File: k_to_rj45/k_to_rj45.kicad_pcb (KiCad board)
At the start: 2 copper layers, 57.2 x 76.2 mm, 13 parts, among them J1 Conn_01x01_Female, J2 Conn_01x01_Female, J3 Conn_01x01_Female, J4 Conn_01x01_Female, J5 Conn_01x01_Female, J6 RJ45_Shielded, J7 Conn_01x01_Female, J8 Conn_01x01_Female, SW1 SW_SPDT

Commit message: rev3 on contact checker boards
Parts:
- added REF**: KiCad-Logo2_5mm_SilkScreen, Symbol:KiCad-Logo2_5mm_SilkScreen, F.Cu at (114.3, 85.7)
- LOGO1, LOGO2: footprint custom_footprints:logo_small -> custom_footprints:logo
- SW1: value SW_SPDT -> SW_SPDT_MSM
- moved LOGO1 13.1 mm to (106.0, 73.0), turned to -90 degrees
- moved LOGO2 13.1 mm to (106.0, 73.0), turned to 90 degrees
- moved REF** 1.27 mm to (114.3, 85.7)
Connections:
- J6 pad 6: GNDPWR -> /GUARD
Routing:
- net /GUARD: track 47.2 -> 70.5 mm
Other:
- board text added: "gXXXXXXX"
- board text removed: "g3d57883"

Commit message: update silk
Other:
- board text added: "gd87d8d8"
- board text removed: "gXXXXXXX"

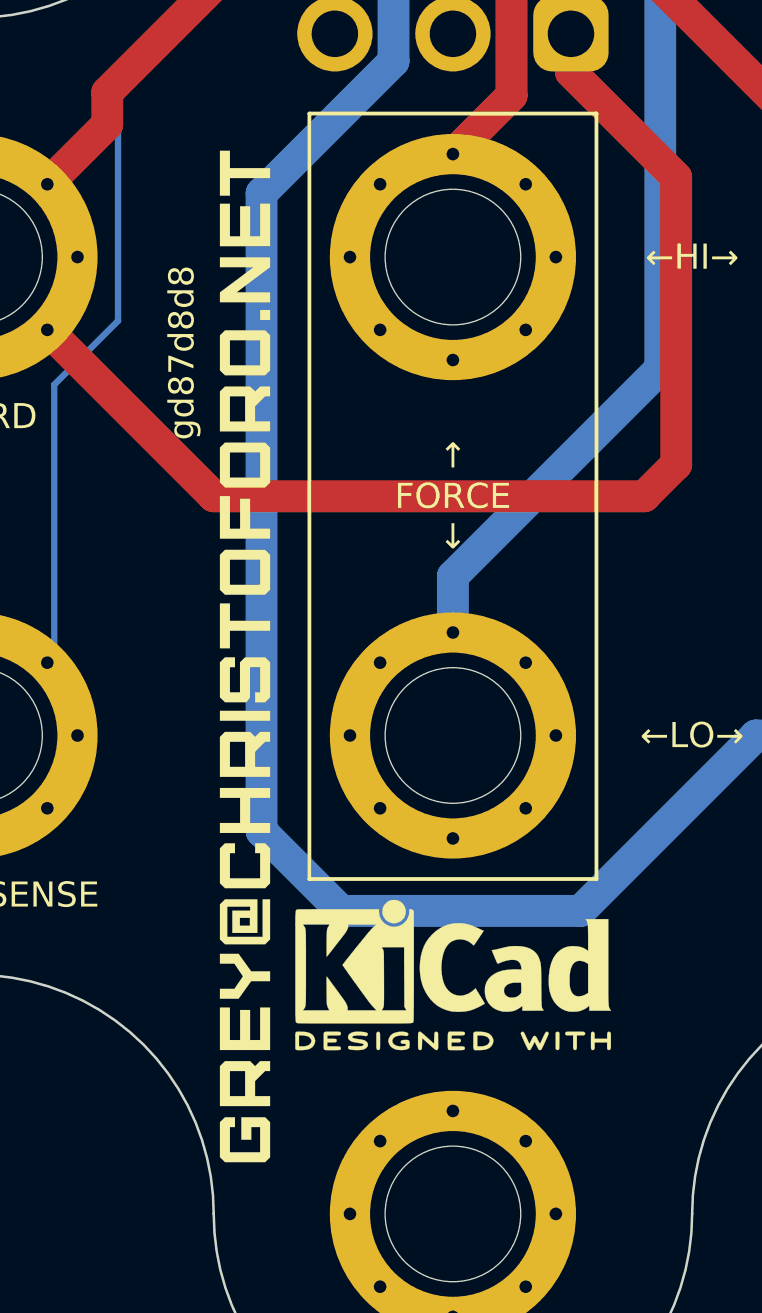
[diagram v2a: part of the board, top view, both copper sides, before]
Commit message: new holder pcbs
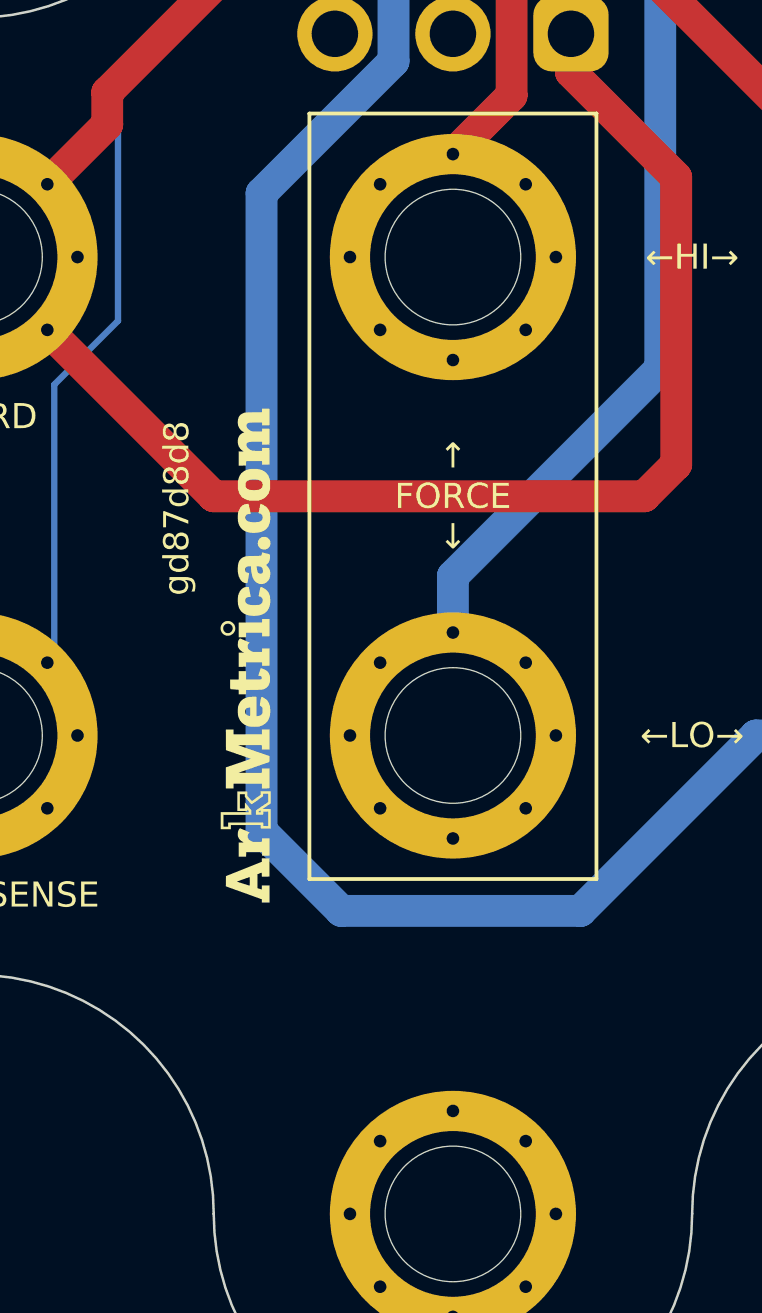
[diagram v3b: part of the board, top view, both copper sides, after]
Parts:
- removed the REF** at (114.3, 85.7) (x2)
- LOGO1, LOGO2: footprint custom_footprints:logo -> custom_footprints:site_small

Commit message: update silk
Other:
- board text added: "b8007ef"
- board text removed: "gd87d8d8"
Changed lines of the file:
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@@
     (effects (font (size 1 1) (thickness 0.15)) (justify mirror))
   )
-  (gr_text "gd87d8d8" (at 103.505 79.15 90) (layer "B.SilkS")
+  (gr_text "b8007ef" (at 103.505 79.15 90) (layer "B.SilkS")
     (effects (font (size 1 1) (thickness 0.15)) (justify mirror))
   )
@@
     (effects (font (size 1 1) (thickness 0.15)))
   )
-  (gr_text "gd87d8d8" (at 103.3 67.15 90) (layer "F.SilkS")
+  (gr_text "b8007ef" (at 103.3 67.15 90) (layer "F.SilkS")
     (effects (font (size 1 1) (thickness 0.15)))
   )

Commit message: fix up rj45 pad numbering
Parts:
- J6: footprint custom_footprints:RJ45_TE_100616-1_vertical_shield -> custom_footprints:RJ45_TE_100616
- LOGO1, LOGO2: footprint custom_footprints:site_small -> custom_footprints:logo
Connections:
- J6 pad 1: /HI_FORCE -> GNDPWR
- J6 pad 2: /HI_SENSE -> GNDPWR
- J6 pad 3: /LO_SENSE -> /GUARD
- J6 pad 4: /LO_FORCE -> /GUARD_SENSE
- J6 pad 5: /GUARD_SENSE -> /LO_FORCE
- J6 pad 6: /GUARD -> /LO_SENSE
- J6 pad 7: GNDPWR -> /HI_SENSE
- J6 pad 8: GNDPWR -> /HI_FORCE

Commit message: shrink steps, add double rj45 to cc
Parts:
- removed REF**: Symbol_Attention_CopperTop_Small, Symbol:Symbol_Attention_CopperTop_Small
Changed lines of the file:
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@@
   (net 7 "/GUARD")
   (net 8 "/SHIELD")
-  (footprint "Symbol:Symbol_Attention_CopperTop_Small" (layer "F.Cu")
-    (at 114.3 34.925)
-    (descr "Symbol, Attention, Copper Top, Small,")
-    (tags "Symbol, Attention, Copper Top, Small,")
-    (attr exclude_from_pos_files exclude_from_bom)
-    (fp_text reference "REF**" (at -0.127 -5.715) (layer "F.SilkS") hide
-        (effects (font (size 1 1) (thickness 0.15)))
-    )
-    (fp_text value "Symbol_Attention_CopperTop_Small" (at -0.381 4.572) (layer "F.Fab")
-        (effects (font (size 1 1) (thickness 0.15)))
-    )
-    (fp_line (start -4.699 2.794) (end 0 -4.191)
-      (stroke (width 0.381) (type solid)) (layer "F.SilkS"))
-    (fp_line (start -0.508 -2.54) (end 0 -2.54)
-      (stroke (width 0.381) (type solid)) (layer "F.SilkS"))
-    (fp_line (start 0 -4.191) (end 4.699 2.794)
-      (stroke (width 0.381) (type solid)) (layer "F.SilkS"))
-    (fp_line (start 0 -2.54) (end 0.508 -2.54)
-      (stroke (width 0.381) (type solid)) (layer "F.SilkS"))
-    (fp_line (start 0 0.889) (end 0.127 -2.54)
-      (stroke (width 0.381) (type solid)) (layer "F.SilkS"))
-    (fp_line (start 0 1.016) (end -0.508 -2.54)
-      (stroke (width 0.381) (type solid)) (layer "F.SilkS"))
-    (fp_line (start 0 1.016) (end -0.127 -2.54)
-      (stroke (width 0.381) (type solid)) (layer "F.SilkS"))
-    (fp_line (start 0.508 -2.54) (end 0 1.016)
-      (stroke (width 0.381) (type solid)) (layer "F.SilkS"))
-    (fp_line (start 4.699 2.794) (end -4.699 2.794)
-      (stroke (width 0.381) (type solid)) (layer "F.SilkS"))
-    (fp_circle (center 0 1.905) (end 0.127 1.905)
-      (stroke (width 0.381) (type solid)) (fill none) (layer "F.SilkS"))
-    (fp_circle (center 0 1.905) (end 0.35921 1.905)
-      (stroke (width 0.381) (type solid)) (fill none) (layer "F.SilkS"))
-  )
   (footprint "custom_footprints:logo" (layer "F.Cu")
     (at 106.045 73.025 90)
